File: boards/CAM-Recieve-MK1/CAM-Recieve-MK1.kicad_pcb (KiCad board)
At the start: 4 copper layers, 208.8 x 83.3 mm, 64 parts, among them J1 SMA, J101 USB4105-GF-A, J107 Conn_01x03, J108 Conn_01x03, J109 Conn_01x03, U1 RF4463PRO, U101 ECMF02-2AMX6, U106 INA745x, U2 TPS63802DLAR, U3 PMA-545G1+, U5 TPSM82813SILR

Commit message: Routing Work!
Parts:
- moved H103 172.4 mm to (48.0, 38.8)
- moved H101 132.1 mm to (90.0, 84.7)
- moved H104 106.5 mm to (90.0, 38.9)
- moved D105 78.7 mm to (81.0, 75.7), turned to -90 degrees
- moved R142 77.9 mm to (81.0, 78.7), turned to 90 degrees
- moved D106 76.5 mm to (82.5, 75.7), turned to -90 degrees
- moved H102 76.4 mm to (128.8, 44.6)
- moved R143 75.7 mm to (82.5, 78.7), turned to 90 degrees
- moved J109 75.0 mm to (45.8, 77.1), turned to 0 degrees
- moved D107 74.1 mm to (81.0, 69.6), turned to -90 degrees
- moved R144 72.9 mm to (81.0, 72.5), turned to 90 degrees
- moved D104 72.2 mm to (82.4, 69.5), turned to -90 degrees
- moved R141 70.9 mm to (82.5, 72.5), turned to 90 degrees
- moved C33 66.5 mm to (68.1, 73.6), turned to 90 degrees
- moved C37 63.0 mm to (72.4, 72.3), turned to 0 degrees
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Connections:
- U7 pad 55: unconnected-(U7-GPIO28-Pad55) -> /SENSE_SCL
- U7 pad 56: /SENSE_ALERT -> /SENSE_SDA
- U7 pad 57: /SENSE_SCL -> /SENSE_ALERT
- U7 pad 58: /SENSE_SDA -> unconnected-(U7-GPIO31-Pad58)
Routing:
- net /RESET_SW: track 3.93 -> 25.0 mm
- net /BOOT_SW: track 0.00 -> 15.7 mm
- net /C6_RESET_SW: track 0.00 -> 15.2 mm
- net +3V3: track 15.7 -> 3.51 mm, vias 3 -> 1
- net /SENSE_ALERT: track 0.00 -> 11.0 mm, vias 0 -> 2
- net /VREG_IN: track 10.4 -> 21.3 mm, vias 2 -> 0
- net +5V: track 5.06 -> 15.9 mm
- net /D+: track 5.85 -> 11.5 mm
- net /Si4463_CS: track 0.00 -> 5.36 mm
- net /SENSE_SCL: track 5.78 -> 10.9 mm, vias 0 -> 2
- net /Si4463_GPIO0: track 0.00 -> 4.11 mm
- net /Si4463_GPIO1: track 0.00 -> 3.76 mm
- net /D-: track 6.52 -> 10.2 mm
- net /USB_D-: track 6.00 -> 2.40 mm
- net /USB_D+: track 5.08 -> 1.79 mm
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- added copper zone on B.Cu, net +3V3
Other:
- board size 208.8 x 83.3 mm -> 50.5 x 53.8 mm

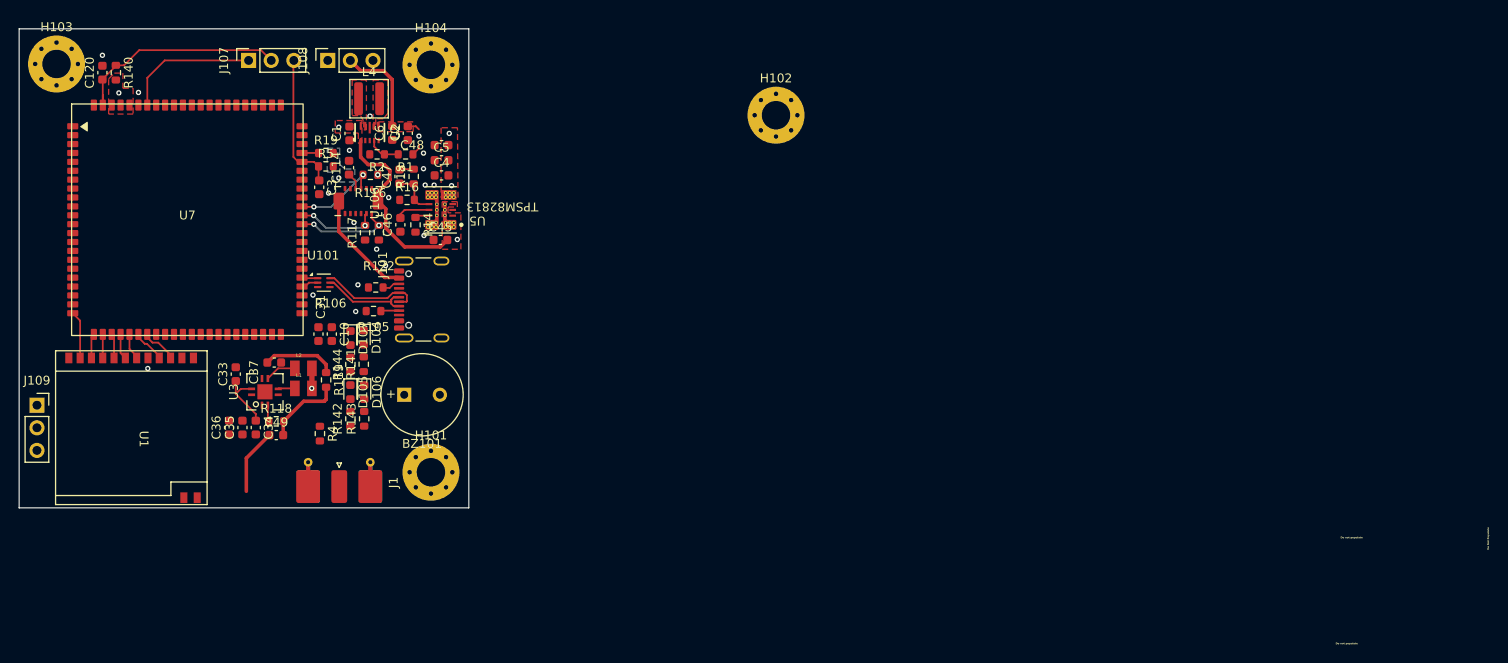
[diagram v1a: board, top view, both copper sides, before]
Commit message: Schematic Fixes, and Lots of Routing Work
- Preliminary Routing finished
- Four board layer routing, zone filling finish.
- Imported 3D models for electronic components
- Changed 3v3 voltage regulator package type.
- Changing some symbols, footprints, 3D model to conventions
- Some DRC checking.
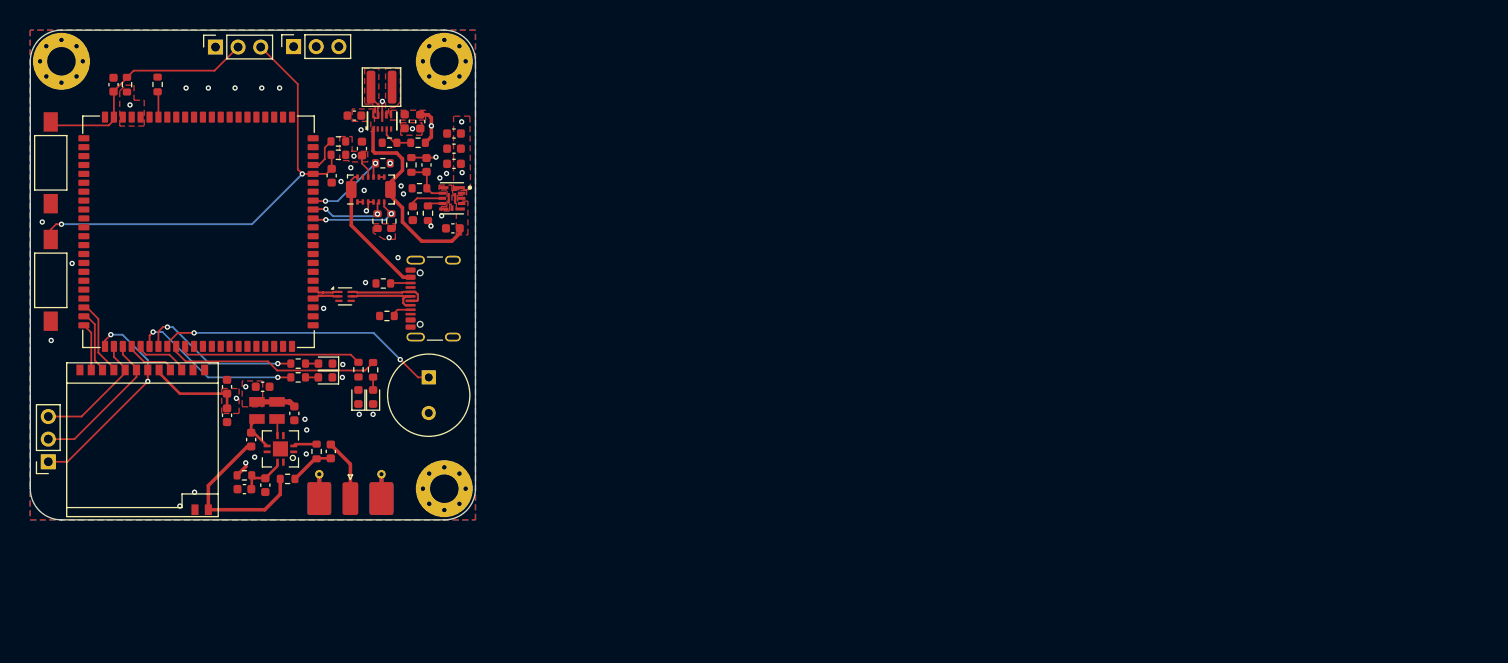
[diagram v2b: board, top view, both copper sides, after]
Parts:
- removed H102: MountingHole, MountingHole:MountingHole_3.2mm_M3_Pad_Via
- added R3: 0, Resistor_SMD:R_0603_1608Metric, F.Cu at (59.3, 41.1)
- added SW2: SW_Push, Button_Switch_SMD:SW_SPST_FSMSM, F.Cu at (47.3, 49.9)
- added SW3: SW_Push, Button_Switch_SMD:SW_SPST_FSMSM, F.Cu at (47.3, 63.1)
- U5: footprint Voltage Regulators:SIL0014B-MFG -> QFN-8 3x3mm:QFN-FCMOD-VCA0013A
- moved C10 14.9 mm to (67.1, 78.2)
- moved C33 12.9 mm to (71.4, 86.1), turned to -90 degrees
- moved R119 11.9 mm to (73.9, 85.4), turned to 0 degrees
- moved C31 11.8 mm to (67.1, 75.0), turned to 90 degrees
- moved R4 9.69 mm to (69.0, 85.0), turned to 180 degrees
- moved C37 9.03 mm to (69.8, 81.0), turned to 90 degrees
- moved R143 8.75 mm to (75.1, 74.0), turned to 0 degrees
- moved C36 7.50 mm to (74.7, 78.0)
- moved L2 7.04 mm to (70.5, 77.7), turned to 90 degrees
- moved C34 7.04 mm to (69.0, 86.5), turned to 180 degrees
- moved D104 6.70 mm to (81.8, 76.2), turned to 90 degrees
- moved U3 6.64 mm to (73.1, 82.0), turned to 180 degrees
- moved J109 6.48 mm to (47.0, 83.5), turned to 180 degrees
- moved C49 6.39 mm to (78.8, 82.3), turned to -90 degrees
- moved R142 6.06 mm to (83.5, 73.2), turned to -90 degrees
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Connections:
- J107 pad 1: /C6_RESET_SW -> GND
- U5 pad 1: /VREG_IN -> +3V3
- U5 pad 10: GND -> unconnected-(U5-PG-Pad10)
- U5 pad 11: Net-(U5-VIN-Pad11) -> /VREG_IN
- U5 pad 12: Net-(U5-VIN-Pad11) -> GND
- U5 pad 13: GND -> /VREG_IN
- U5 pad 2: /VREG_IN -> GND
- U5 pad 3: unconnected-(U5-PG-Pad3) -> Net-(U5-FB)
- U5 pad 4: /VREG_IN -> Net-(U5-SS_TR)
- U5 pad 5: +3V3 -> Net-(U5-COMP_FSET)
- U5 pad 7: Net-(U5-FB) -> unconnected-(U5-SW-Pad7)
- U5 pad 8: Net-(U5-SS_TR) -> /VREG_IN
- U5 pad 9: Net-(U5-COMP_FSET) -> /VREG_IN
- U7 pad 20: unconnected-(U7-GPIO5-Pad20) -> /Si4463_nSEL
- U7 pad 21: unconnected-(U7-GPIO6-Pad21) -> /Si4463_nIRQ
- U7 pad 23: /Si4463_nIRQ -> /SPI_MISO
- U7 pad 24: /Si4463_nSEL -> /SPI_SCK
- U7 pad 25: /SPI_SCK -> /SPI_MOSI
- U7 pad 26: /SPI_MOSI -> /Si4463_GPIO1
- U7 pad 27: /SPI_MISO -> /Si4463_GPIO0
- U7 pad 28: /Si4463_GPIO1 -> /LED_GREEN
- U7 pad 29: /Si4463_GPIO0 -> /LED_BLUE
- U7 pad 30: /LED_ORANGE -> /BUZZER
- U7 pad 31: /BUZZER -> /LED_ORANGE
- U7 pad 55: /SENSE_SCL -> unconnected-(U7-GPIO28-Pad55)
- U7 pad 56: /SENSE_SDA -> unconnected-(U7-GPIO29-Pad56)
- U7 pad 57: /SENSE_ALERT -> /SENSE_SCL
- U7 pad 58: unconnected-(U7-GPIO31-Pad58) -> /SENSE_SDA
- U7 pad 59: unconnected-(U7-GPIO32-Pad59) -> /SENSE_ALERT
- U7 pad 80: /LED_GREEN -> unconnected-(U7-GPIO52-Pad80)
- U7 pad 81: /LED_BLUE -> unconnected-(U7-GPIO53-Pad81)
- U7 pad 82: /C6_RESET_SW -> Net-(U7-GPIO54)
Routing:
- net +5V: track 15.9 -> 74.6 mm, vias 1 -> 3
- net /BOOT_SW: track 15.7 -> 54.0 mm, vias 0 -> 2
- net /BUZZER: track 0.00 -> 32.8 mm, vias 0 -> 2
- net /LED_ORANGE: track 0.00 -> 24.0 mm
- net /SPI_MISO: track 2.98 -> 25.8 mm, vias 0 -> 2
- net /LED_RED: track 0.00 -> 20.6 mm
- net /LED_GREEN: track 0.14 -> 19.4 mm, vias 0 -> 2
- net /LED_BLUE: track 0.00 -> 18.4 mm, vias 0 -> 2
- net /C6_RESET_SW: track 15.2 -> 0.00 mm
- net /SPI_MOSI: track 2.87 -> 17.2 mm
- net +3V3: track 3.51 -> 16.0 mm, vias 1 -> 8
- net /Si4463_ANT: track 8.24 -> 19.9 mm
- net /SPI_SCK: track 2.75 -> 14.2 mm
- net /Si4463_nSEL: track 2.65 -> 8.61 mm
- net /Si4463_nIRQ: track 2.82 -> 7.09 mm
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- added copper zone on In2.Cu, net +3V3
- added copper zone on B.Cu, net GND
- added copper zone on F.Cu, net GND
- added copper zone on In1.Cu, net GND
- added copper zone on F.Cu, net Net-(U2-L1)
- added copper zone on F.Cu, net Net-(U2-L2)
- removed copper zone on F.Cu, net (none)
- removed copper zone on B.Cu, net +3V3
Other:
- board size 50.5 x 53.8 mm -> 50 x 55 mm
- board text removed: "Do Not Populate"
- board text removed: "Do not populate"

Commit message: Library Conventions
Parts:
- removed U3: PMA-545G1+, QFN-8 3x3mm:QFN-8 3x3mm
- added U4: PMA-545G1+, QFN-8 3x3mm:QFN-8 3x3mm, F.Cu at (73.0, 82.1)
- U2: value TPS63802DLAR -> TPS63802

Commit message: DRC Passed!
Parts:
- L1, L2: footprint Murata_Electronics_Inductors:Murata_0805_2015 -> Inductor_SMD:L_0805_2012Metric
- U1: footprint RF_Module:RF4463PRO -> RF_Module_NiceRF:RF4463PRO
- U2: footprint Voltage Regulators:DLA0010A -> Package_DFN:DLA0010A
- U7: footprint ESP32_P4_Module:ESP32-P4-Module-Waveshare -> MCU_ESP32:ESP32-P4-Module-Waveshare
- moved C1 0.46 mm to (81.0, 44.5)
- moved C6 0.21 mm to (87.2, 45.3)
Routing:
- net /SYS_POWER: track 15.1 -> 21.8 mm
- net Net-(D104-A): track 0.00 -> 1.46 mm

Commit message: Little Touches
- Footprints Graphics Uploaded.
- Names Added
- Fix with 3D Model
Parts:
- added G***: LOGO, Logos_ISS:ISS_LOGOV2_tiny, F.Cu at (85.7, 81.5)
- added G***: LOGO, Memes:UIUC_small, F.Cu at (70.5, 41.2)
- added G***: LOGO, Memes:griffen, F.Cu at (126.6, 59.9)
- added G***: LOGO, Memes:Eagle, B.Cu at (69.4, 59.9)
- moved BZ101 0.63 mm to (89.8, 73.4)
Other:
- board text added: "Thomas McManamen, Chethan Karandikar, Rohan Das, Kacper Paraniuk, Eddie Tang, Andrew Dorman, Azalea Shillington, Mason Miao, Mike Hung, Sahir Pagey"

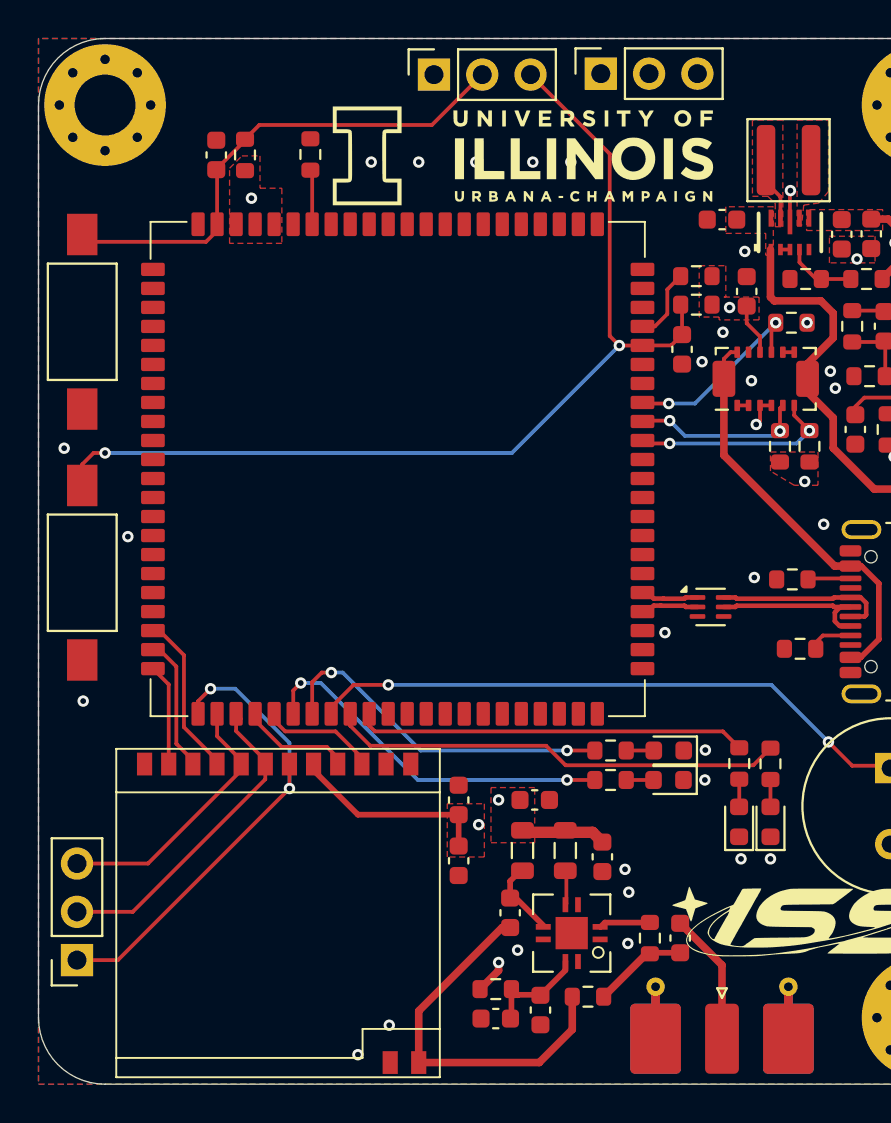
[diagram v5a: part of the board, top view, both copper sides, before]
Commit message: New 3D Model for RF4463 and Silkscreen Additions
- Named pins outs with silkscreen
- New 3D Model.
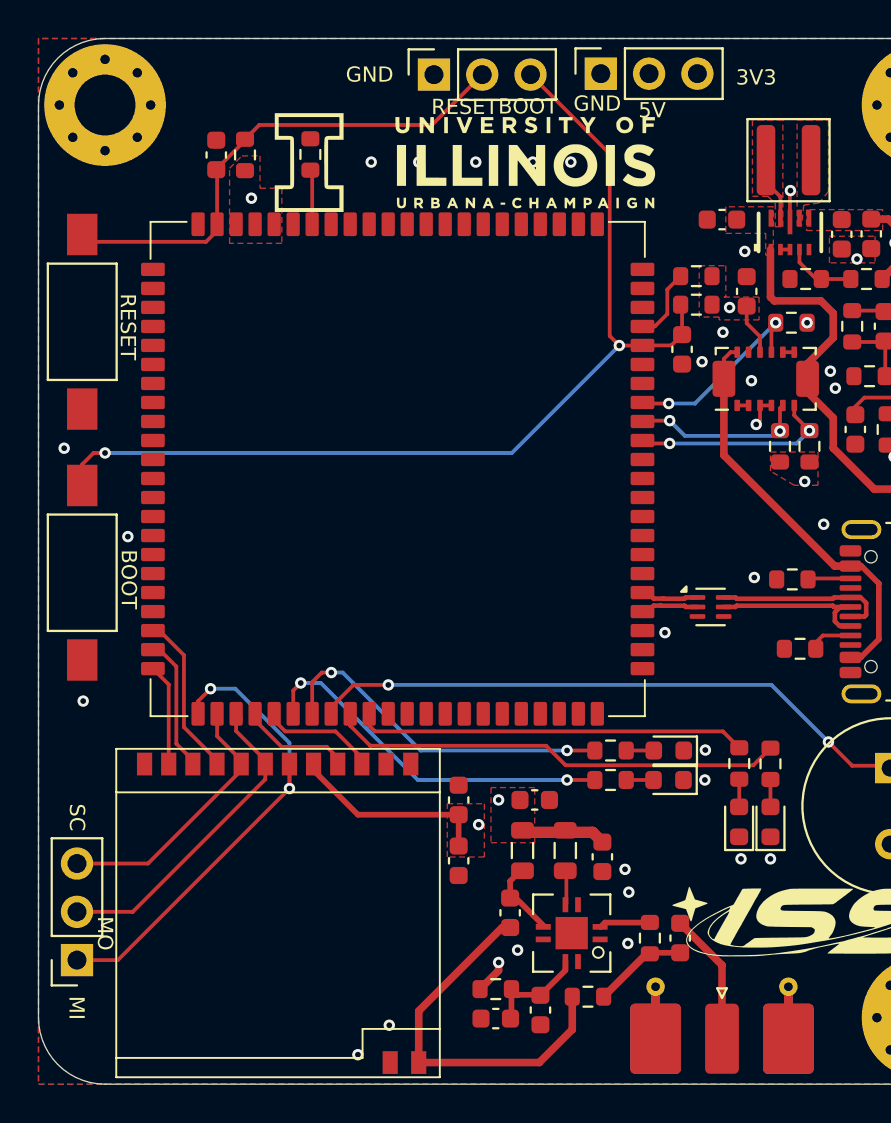
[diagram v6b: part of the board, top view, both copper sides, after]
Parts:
- moved G*** 3.07 mm to (67.4, 41.5)
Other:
- board text added: "3V3"
- board text added: "5V"
- board text added: "BOOT"
- board text added: "GND"
- board text added: "Kacper Paraniuk, Rohan Das, Thomas McManamen, Chethan Karandikar, Eddie Tang, Andrew Dorman, Azalea Shillington, Mason Miao, Mike Hung, Sahir Pagey"
- board text added: "MI"
- board text added: "MO"
- board text added: "RESET"
- board text added: "SC"
- board text removed: "Thomas McManamen, Chethan Karandikar, Rohan Das, Kacper Paraniuk, Eddie Tang, Andrew Dorman, Azalea Shillington, Mason Miao, Mike Hung, Sahir Pagey"
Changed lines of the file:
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@@
 	(footprint "Memes:UIUC_small"
 		(layer "F.Cu")
-		(at 70.475 41.175)
+		(at 67.425 41.525)
 		(property "Reference" "G***"
 			(at 0 0 0)
@@
 				(keep_text_aligned yes)
 			)
-			(gr_text "618.1102"
+			(gr_text "15.7"
 				(at 67.372 81.0125 90)
 				(layer "Dwgs.User")
@@
 				(keep_text_aligned yes)
 			)
-			(gr_text "43.7008"
+			(gr_text "1.11"
 				(at 65.554 103.3435 0)
 				(layer "Dwgs.User")
@@
 				(keep_text_aligned yes)
 			)
-			(gr_text "551.1811"
+			(gr_text "14"
 				(at 57.579 61.8145 0)
 				(layer "Dwgs.User")
@@
 				(keep_text_aligned yes)
 			)
-			(gr_text "57.874"
+			(gr_text "1.47"
 				(at 49.844 64.7355 0)
 				(layer "Dwgs.User")
@@
 				(keep_text_aligned yes)
 			)
-			(gr_text "50"
+			(gr_text "1.27"
 				(at 51.214 68.0375 0)
 				(layer "Dwgs.User")
@@
 				(keep_text_aligned yes)
 			)
-			(gr_text "681.1024"
+			(gr_text "17.3"
 				(at 69.959 81.0125 90)
 				(layer "Dwgs.User")
@@
 				(keep_text_aligned yes)
 			)
-			(gr_text "60.2362"
+			(gr_text "1.53"
 				(at 65.344 60.9255 0)
 				(layer "Dwgs.User")
@@
 				(keep_text_aligned yes)
 			)
-			(gr_text "59.0551"
+			(gr_text "1.5"
 				(at 64.249 100.5495 0)
 				(layer "Dwgs.User")
@@
 				(keep_text_aligned yes)
 			)
-			(gr_text "669.2913"
+			(gr_text "17"
 				(at 57.609 93.7125 0)
 				(layer "Dwgs.User")
@@
 		(layer "Edge.Cuts")
 	)
-	(gr_text "Thomas McManamen, Chethan Karandikar, Rohan Das, \nKacper Paraniuk, Eddie Tang, Andrew Dorman, \nAzalea Shillington, Mason Miao, Mike Hung, Sahir Pagey"
-		(at 74.575 88.75 -0)
+	(gr_text "RESET\n"
+		(at 69.175 38.6 0)
+		(layer "F.SilkS")
+		(effects
+			(font
+				(size 0.8 0.8)
+				(thickness 0.15)
+			)
+			(justify right)
+		)
+	)
+	(gr_text "5V"
+		(at 78 38.775 0)
+		(layer "F.SilkS")
+		(effects
+			(font
+				(size 0.8 0.8)
+				(thickness 0.15)
+			)
+			(justify right)
+		)
+	)
+	(gr_text "BOOT"
+		(at 72.325 38.575 0)
+		(layer "F.SilkS")
+		(effects
+			(font
+				(size 0.8 0.8)
+				(thickness 0.15)
+			)
+			(justify right)
+		)
+	)
+	(gr_text "RESET"
+		(at 49.7 51.925 270)
+		(layer "F.SilkS")
+		(effects
+			(font
+				(size 0.8 0.8)
+				(thickness 0.15)
+			)
+			(justify right)
+		)
+	)
+	(gr_text "SC"
+		(at 47.025 76.7 270)
+		(layer "F.SilkS")
+		(effects
+			(font
+				(size 0.8 0.8)
+				(thickness 0.15)
+			)
+			(justify right)
+		)
+	)
+	(gr_text "BOOT"
+		(at 49.75 65.025 270)
+		(layer "F.SilkS")
+		(effects
+			(font
+				(size 0.8 0.8)
+				(thickness 0.15)
+			)
+			(justify right)
+		)
+	)
+	(gr_text "MO"
+		(at 48.5 82.975 270)
+		(layer "F.SilkS")
+		(effects
+			(font
+				(size 0.8 0.8)
+				(thickness 0.15)
+			)
+			(justify right)
+		)
+	)
+	(gr_text "GND"
+		(at 75.65 38.425 0)
+		(layer "F.SilkS")
+		(effects
+			(font
+				(size 0.8 0.8)
+				(thickness 0.15)
+			)
+			(justify right)
+		)
+	)
+	(gr_text "GND"
+		(at 63.675 36.9 0)
+		(layer "F.SilkS")
+		(effects
+			(font
+				(size 0.8 0.8)
+				(thickness 0.15)
+			)
+			(justify right)
+		)
+	)
+	(gr_text "MI"
+		(at 47 86.625 270)
+		(layer "F.SilkS")
+		(effects
+			(font
+				(size 0.8 0.8)
+				(thickness 0.15)
+			)
+			(justify right)
+		)
+	)
+	(gr_text "3V3"
+		(at 83.825 37.05 0)
+		(layer "F.SilkS")
+		(effects
+			(font
+				(size 0.8 0.8)
+				(thickness 0.15)
+			)
+			(justify right)
+		)
+	)
+	(gr_text "Kacper Paraniuk, Rohan Das, Thomas McManamen, Chethan Karandikar, \nEddie Tang, Andrew Dorman, Azalea Shillington, \nMason Miao, Mike Hung, Sahir Pagey"
+		(at 75.2 88.825 0)
 		(layer "B.SilkS")
 		(effects
